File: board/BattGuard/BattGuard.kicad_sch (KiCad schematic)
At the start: 160 parts, among them J1 OQ0271510000G, J10 Conn_01x01_Pin, J11 Conn_01x01_Pin, J12 Conn_01x01_Pin, J13 Conn_01x01_Pin, J14 Conn_01x01_Pin, J15 Conn_01x01_Pin, J17 S5B-XH-A, J18 FAN1 5V, J19 FAN2 5V, J2 Barrel_Jack, J3 Conn_01x22_Pin, J4 Conn_01x22_Pin, J5 Conn_01x02_Pin(xt60), J6 OLED DISPLAY, J7 EC5 JUMP CONNECTOR, J8 GSB4111312HR, J9 Conn_01x01_Pin, Q1 SIR680LDP-T1-RE3, Q2 SIR680LDP-T1-RE3, Q3 SIR680LDP-T1-RE3, Q4 SIR680LDP-T1-RE3, Q5 Q_PMOS_DGS, Q7 AO3401A, Q8 2N7002, SW1 SW_Push, SW2 SW_Push, U1 BQ25756ERRVR, U2 LMR51420XDDCR, U3 MCP45HV51-ST, U4 INA226, U5 LM317_TO3, U6 TLV76133KVUR, U7 TLV61047DDC

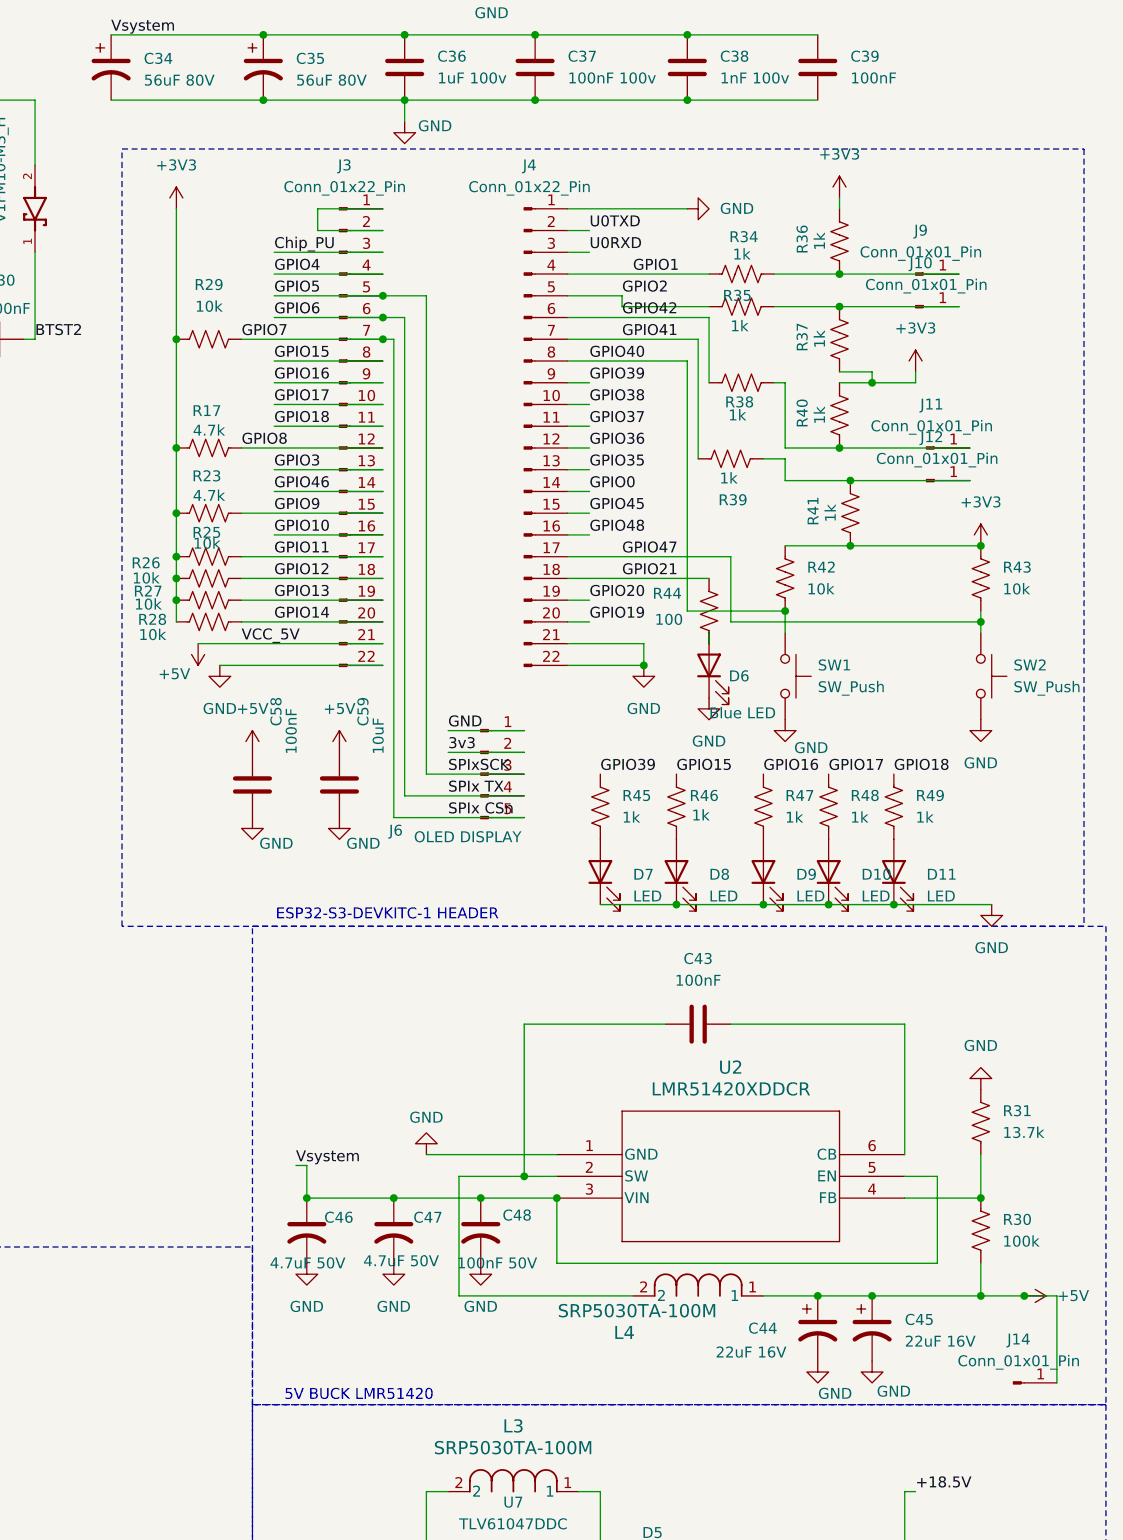
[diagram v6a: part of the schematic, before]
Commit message: 10.29.2026 Night
Routed ALL GPIO Traces from bq and other perhpirals, moved fan pads to oppsite sides of boards, fixed LED pads,
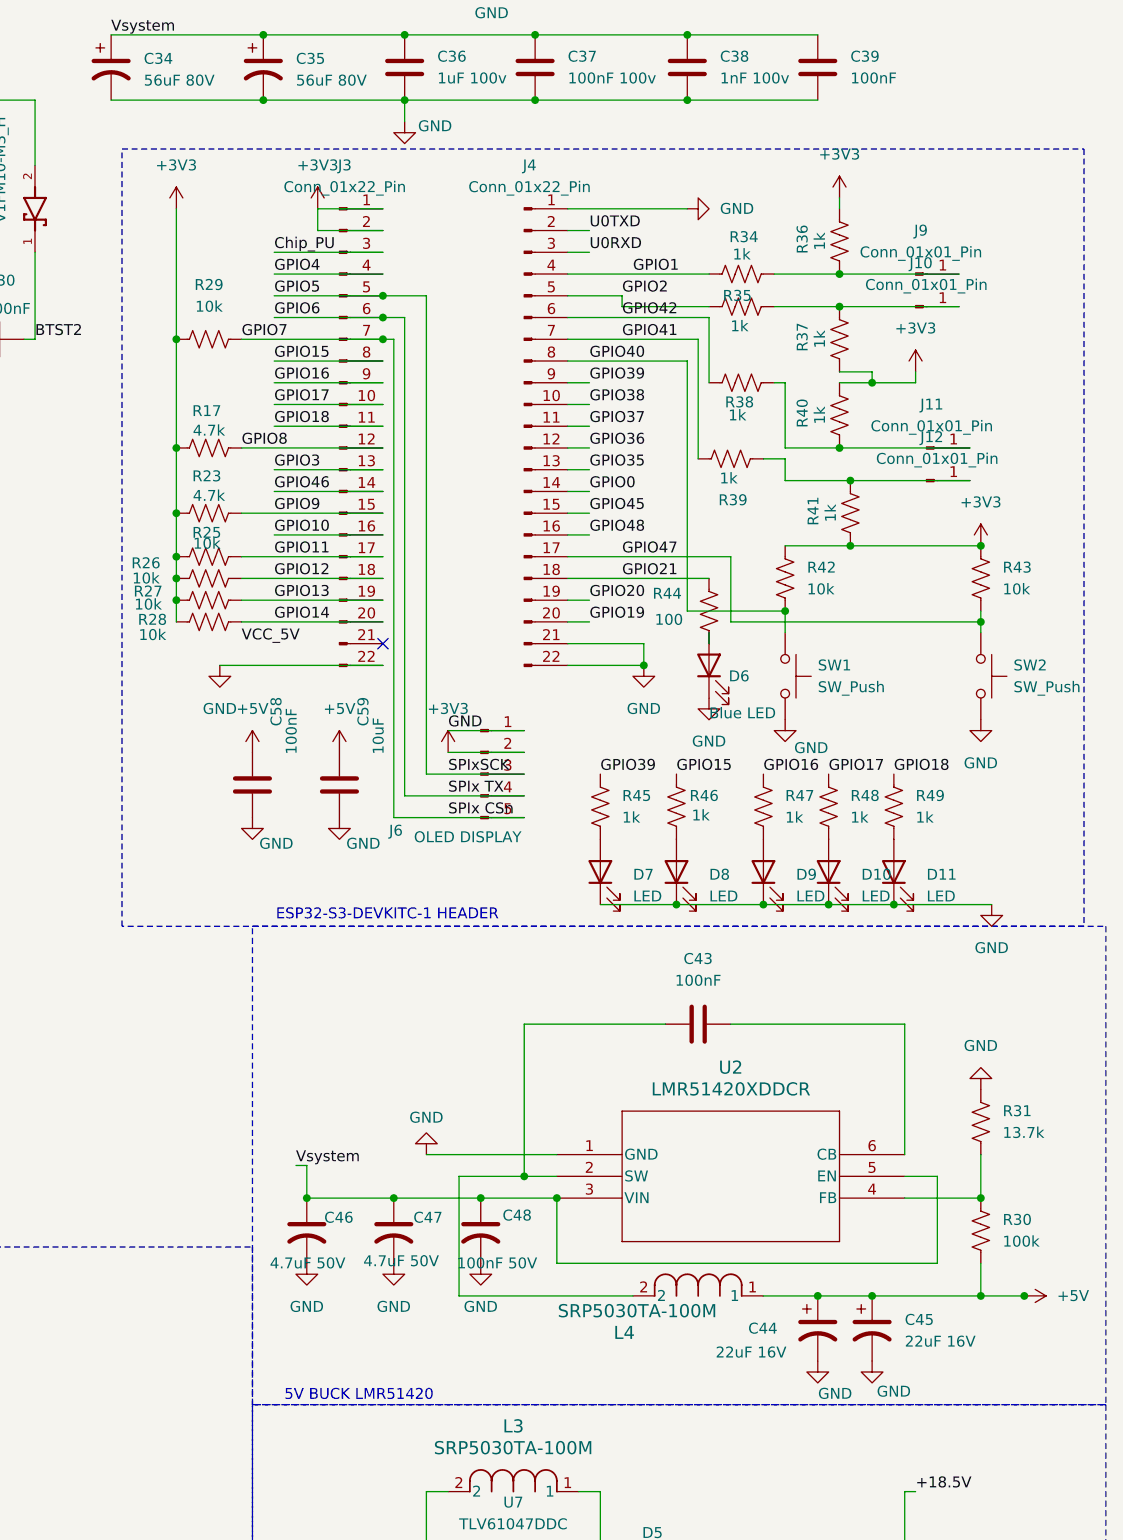
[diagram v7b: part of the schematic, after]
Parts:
- removed J14: Conn_01x01_Pin, TestPoint:TestPoint_Pad_1.0x1.0mm, symbol Connector:Conn_01x01_Pin
- D10, D11, D7, D8, D9: footprint LED_THT:LED_D1.8mm_W1.8mm_H2.4mm_Horizontal_O1.27mm_Z4.9mm -> TeamLib:Wire_Pads_1x02_SMD_2.54
- D6: footprint TestPoint:TestPoint_Pad_1.0x1.0mm -> TeamLib:Wire_Pads_1x02_SMD_2.54
- SW1, SW2: footprint (none) -> TeamLib:Wire_Pads_1x02_SMD_2.54
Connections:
- net 3v3 is gone; now on net +3V3: J6.2 (Pin_2)
- net +3V3: now also J3.1 (Pin_1), J3.2 (Pin_2)
- net +5V: no longer J3.21 (Pin_21)
- no-connect marks 6 -> 7
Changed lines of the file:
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@@
 	)
 	(no_connect
+		(at 322.58 118.11)
+	)
+	(no_connect
 		(at 161.29 105.41)
 	)
@@
 	(wire
 		(pts
-			(xy 401.32 204.47) (xy 401.32 194.31)
-		)
-		(stroke
-			(width 0)
-			(type default)
-		)
-	)
-	(wire
-		(pts
 			(xy 335.28 36.83) (xy 335.28 39.37)
 		)
@@
 	(wire
 		(pts
-			(xy 300.99 118.11) (xy 322.58 118.11)
-		)
-		(stroke
-			(width 0)
-			(type default)
-		)
-	)
-	(wire
-		(pts
 			(xy 88.9 22.86) (xy 102.87 22.86)
 		)
@@
 	(wire
 		(pts
-			(xy 401.32 194.31) (xy 397.51 194.31)
-		)
-		(stroke
-			(width 0)
-			(type default)
-		)
-	)
-	(wire
-		(pts
 			(xy 68.58 240.03) (xy 68.58 236.22)
 		)
@@
 		)
 	)
-	(label "3v3"
-		(at 330.2 130.81 0)
-		(effects
-			(font
-				(size 1.27 1.27)
-			)
-			(justify left bottom)
-		)
-	)
 	(label "LODRV2"
 		(at 254 101.6 0)
@@
 	)
 	(symbol
+		(lib_id "power:+3V3")
+		(at 330.2 130.81 0)
+		(unit 1)
+		(body_style 1)
+		(exclude_from_sim no)
+		(in_bom yes)
+		(on_board yes)
+		(in_pos_files yes)
+		(dnp no)
+		(fields_autoplaced yes)
+		(property "Reference" "#PWR090"
+			(at 330.2 134.62 0)
+			(hide yes)
+			(show_name no)
+			(do_not_autoplace no)
+			(effects
+				(font
+					(size 1.27 1.27)
+				)
+			)
+		)
+		(property "Value" "+3V3"
+			(at 330.2 125.73 0)
+			(show_name no)
+			(do_not_autoplace no)
+			(effects
+				(font
+					(size 1.27 1.27)
+				)
+			)
+		)
+		(property "Footprint" ""
+			(at 330.2 130.81 0)
+			(hide yes)
+			(show_name no)
+			(do_not_autoplace no)
+			(effects
+				(font
+					(size 1.27 1.27)
+				)
+			)
+		)
+		(property "Datasheet" ""
+			(at 330.2 130.81 0)
+			(hide yes)
+			(show_name no)
+			(do_not_autoplace no)
+			(effects
+				(font
+					(size 1.27 1.27)
+				)
+			)
+		)
+		(property "Description" "Power symbol creates a global label with name \"+3V3\""
+			(at 330.2 130.81 0)
+			(hide yes)
+			(show_name no)
+			(do_not_autoplace no)
+			(effects
+				(font
+					(size 1.27 1.27)
+				)
+			)
+		)
+		(pin "1"
+		)
+		(instances
+			(project "BattGuard"
+				(path "/236cbdd7-d83d-4a8e-9ca8-a6b8cdb61d8b"
+					(reference "#PWR090")
+					(unit 1)
+				)
+			)
+		)
+	)
+	(symbol
 		(lib_id "Device:C")
 		(at 307.34 134.62 0)
@@
 			)
 		)
-		(property "Footprint" "LED_THT:LED_D1.8mm_W1.8mm_H2.4mm_Horizontal_O1.27mm_Z4.9mm"
+		(property "Footprint" "TeamLib:Wire_Pads_1x02_SMD_2.54"
 			(at 356.87 144.78 0)
 			(hide yes)
@@
 	)
 	(symbol
-		(lib_id "power:+5V")
-		(at 300.99 118.11 180)
-		(unit 1)
-		(body_style 1)
-		(exclude_from_sim no)
-		(in_bom yes)
-		(on_board yes)
-		(in_pos_files yes)
-		(dnp no)
-		(property "Reference" "#PWR060"
-			(at 300.99 114.3 0)
-			(hide yes)
-			(show_name no)
-			(do_not_autoplace no)
-			(effects
-				(font
-					(size 1.27 1.27)
-				)
-			)
-		)
-		(property "Value" "+5V"
-			(at 298.196 121.666 0)
-			(show_name no)
-			(do_not_autoplace no)
-			(effects
-				(font
-					(size 1.27 1.27)
-				)
-			)
-		)
-		(property "Footprint" ""
-			(at 300.99 118.11 0)
-			(hide yes)
-			(show_name no)
-			(do_not_autoplace no)
-			(effects
-				(font
-					(size 1.27 1.27)
-				)
-			)
-		)
-		(property "Datasheet" ""
-			(at 300.99 118.11 0)
-			(hide yes)
-			(show_name no)
-			(do_not_autoplace no)
-			(effects
-				(font
-					(size 1.27 1.27)
-				)
-			)
-		)
-		(property "Description" "Power symbol creates a global label with name \"+5V\""
-			(at 300.99 118.11 0)
-			(hide yes)
-			(show_name no)
-			(do_not_autoplace no)
-			(effects
-				(font
-					(size 1.27 1.27)
-				)
-			)
-		)
-		(pin "1"
-		)
-		(instances
-			(project "BattGuard"
-				(path "/236cbdd7-d83d-4a8e-9ca8-a6b8cdb61d8b"
-					(reference "#PWR060")
-					(unit 1)
-				)
-			)
-		)
-	)
-	(symbol
 		(lib_id "Device:C_Polarized_US")
 		(at 21.59 139.7 0)
@@
 			)
 		)
-		(property "Footprint" "LED_THT:LED_D1.8mm_W1.8mm_H2.4mm_Horizontal_O1.27mm_Z4.9mm"
+		(property "Footprint" "TeamLib:Wire_Pads_1x02_SMD_2.54"
 			(at 382.27 144.78 0)
 			(hide yes)
@@
 			)
 		)
-		(property "Footprint" ""
+		(property "Footprint" "TeamLib:Wire_Pads_1x02_SMD_2.54"
 			(at 397.51 121.92 0)
 			(hide yes)
@@
 			)
 		)
-		(property "Footprint" "LED_THT:LED_D1.8mm_W1.8mm_H2.4mm_Horizontal_O1.27mm_Z4.9mm"
+		(property "Footprint" "TeamLib:Wire_Pads_1x02_SMD_2.54"
 			(at 374.65 144.78 0)
 			(hide yes)
@@
 			)
 		)
-		(property "Footprint" "LED_THT:LED_D1.8mm_W1.8mm_H2.4mm_Horizontal_O1.27mm_Z4.9mm"
+		(property "Footprint" "TeamLib:Wire_Pads_1x02_SMD_2.54"
 			(at 347.98 144.78 0)
 			(hide yes)
@@
 			)
 		)
-		(property "Footprint" "LED_THT:LED_D1.8mm_W1.8mm_H2.4mm_Horizontal_O1.27mm_Z4.9mm"
+		(property "Footprint" "TeamLib:Wire_Pads_1x02_SMD_2.54"
 			(at 367.03 144.78 0)
 			(hide yes)
@@
 			)
 		)
-		(property "Footprint" "TestPoint:TestPoint_Pad_1.0x1.0mm"
+		(property "Footprint" "TeamLib:Wire_Pads_1x02_SMD_2.54"
 			(at 360.68 120.65 0)
 			(hide yes)
@@
 			)
 		)
-		(property "Footprint" ""
+		(property "Footprint" "TeamLib:Wire_Pads_1x02_SMD_2.54"
 			(at 374.65 121.92 0)
 			(hide yes)
@@
 	)
 	(symbol
+		(lib_id "power:+3V3")
+		(at 314.96 67.31 0)
+		(unit 1)
+		(body_style 1)
+		(exclude_from_sim no)
+		(in_bom yes)
+		(on_board yes)
+		(in_pos_files yes)
+		(dnp no)
+		(fields_autoplaced yes)
+		(property "Reference" "#PWR089"
+			(at 314.96 71.12 0)
+			(hide yes)
+			(show_name no)
+			(do_not_autoplace no)
+			(effects
+				(font
+					(size 1.27 1.27)
+				)
+			)
+		)
+		(property "Value" "+3V3"
+			(at 314.96 62.23 0)
+			(show_name no)
+			(do_not_autoplace no)
+			(effects
+				(font
+					(size 1.27 1.27)
+				)
+			)
+		)
+		(property "Footprint" ""
+			(at 314.96 67.31 0)
+			(hide yes)
+			(show_name no)
+			(do_not_autoplace no)
+			(effects
+				(font
+					(size 1.27 1.27)
+				)
+			)
+		)
+		(property "Datasheet" ""
+			(at 314.96 67.31 0)
+			(hide yes)
+			(show_name no)
+			(do_not_autoplace no)
+			(effects
+				(font
+					(size 1.27 1.27)
+				)
+			)
+		)
+		(property "Description" "Power symbol creates a global label with name \"+3V3\""
+			(at 314.96 67.31 0)
+			(hide yes)
+			(show_name no)
+			(do_not_autoplace no)
+			(effects
+				(font
+					(size 1.27 1.27)
+				)
+			)
+		)
+		(pin "1"
+		)
+		(instances
+			(project "BattGuard"
+				(path "/236cbdd7-d83d-4a8e-9ca8-a6b8cdb61d8b"
+					(reference "#PWR089")
+					(unit 1)
+				)
+			)
+		)
+	)
+	(symbol
 		(lib_id "Device:R_US")
 		(at 57.15 125.73 90)
@@
 					(unit 1)
 				)
-			)
-		)
-	)
-	(symbol
-		(lib_id "Connector:Conn_01x01_Pin")
-		(at 396.24 204.47 0)
-		(unit 1)
-		(body_style 1)
-		(exclude_from_sim no)
-		(in_bom yes)
-		(on_board yes)
-		(in_pos_files yes)
-		(dnp no)
-		(fields_autoplaced yes)
-		(property "Reference" "J14"
-			(at 396.875 199.39 0)
-			(show_name no)
-			(do_not_autoplace no)
-			(effects
-				(font
-					(size 1.27 1.27)
-				)
-			)
-		)
-		(property "Value" "Conn_01x01_Pin"
-			(at 396.875 201.93 0)
-			(show_name no)
-			(do_not_autoplace no)
-			(effects
-				(font
-					(size 1.27 1.27)
-				)
-			)
-		)
-		(property "Footprint" "TestPoint:TestPoint_Pad_1.0x1.0mm"
-			(at 396.24 204.47 0)
-			(hide yes)
-			(show_name no)
-			(do_not_autoplace no)
-			(effects
-				(font
-					(size 1.27 1.27)
-				)
-			)
-		)
-		(property "Datasheet" ""
-			(at 396.24 204.47 0)
-			(hide yes)
-			(show_name no)
-			(do_not_autoplace no)
-			(effects
-				(font
-					(size 1.27 1.27)
-				)
-			)
-		)
-		(property "Description" "Generic connector, single row, 01x01, script generated"
-			(at 396.24 204.47 0)
-			(hide yes)
-			(show_name no)
-			(do_not_autoplace no)
-			(effects
-				(font
-					(size 1.27 1.27)
-				)
-			)
-		)
-		(pin "1"
-		)
-		(instances
-			(project "BattGuard"
-				(path "/236cbdd7-d83d-4a8e-9ca8-a6b8cdb61d8b"
-					(reference "J14")
-					(unit 1)
-				)

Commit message: Routed more traces around the MOSFET switch
Upsized traces etc.
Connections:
- net +18.5V: no longer U3.14 (V+)
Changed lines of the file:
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@@
 	)
 	(junction
-		(at 41.91 204.47)
-		(diameter 0)
-		(color 0 0 0 0)
-	)
-	(junction
 		(at 246.38 213.36)
 		(diameter 0)
@@
 	)
 	(junction
-		(at 397.51 194.31)
-		(diameter 0)
-		(color 0 0 0 0)
-	)
-	(junction
 		(at 160.02 204.47)
 		(diameter 0)
@@
 	(wire
 		(pts
-			(xy 41.91 236.22) (xy 41.91 204.47)
-		)
-		(stroke
-			(width 0)
-			(type default)
-		)
-	)
-	(wire
-		(pts
 			(xy 229.87 198.12) (xy 229.87 195.58)
 		)
@@
 	(wire
 		(pts
-			(xy 41.91 204.47) (xy 49.53 204.47)
+			(xy 39.37 204.47) (xy 49.53 204.47)
 		)
 		(stroke
@@
 	(wire
 		(pts
-			(xy 39.37 204.47) (xy 41.91 204.47)
-		)
-		(stroke
-			(width 0)
-			(type default)
-		)
-	)
-	(wire
-		(pts
 			(xy 73.66 120.65) (xy 60.96 120.65)
 		)
@@
 	(wire
 		(pts
-			(xy 68.58 236.22) (xy 41.91 236.22)
-		)
-		(stroke
-			(width 0)
-			(type default)
-		)
-	)
-	(wire
-		(pts
 			(xy 39.37 157.48) (xy 39.37 171.45)
 		)
@@
 	(wire
 		(pts
-			(xy 68.58 240.03) (xy 68.58 236.22)
-		)
-		(stroke
-			(width 0)
-			(type default)
-		)
-	)
-	(wire
-		(pts
 			(xy 397.51 194.31) (xy 392.43 194.31)
 		)
@@
 			)
 		)
-		(property "Datasheet" ""
+		(property "Datasheet" "file://C:\\Users\\Fluff\\OneDrive\\Documents\\GitHub\\BattGuard\\board\\Datasheets\\DMP6023LSS - PMOS.pdf"
 			(at 66.04 22.86 0)
 			(hide yes)
